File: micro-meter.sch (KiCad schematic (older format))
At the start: 143 parts, among them J1 DC_IN, J10 5V_OUT, J2 SPI, J3 I2C / UART, J4 IN1, J5 IN2, J6 IN3, J7 IN4, J8 SWD, J9 USB_B_Micro, U1 MP2359, U2 STM32F411CEU6, U3 XC6206P332MR, U4 MCP6002-ISN, U5 USBLC6-2SC6, Y1 16MHz

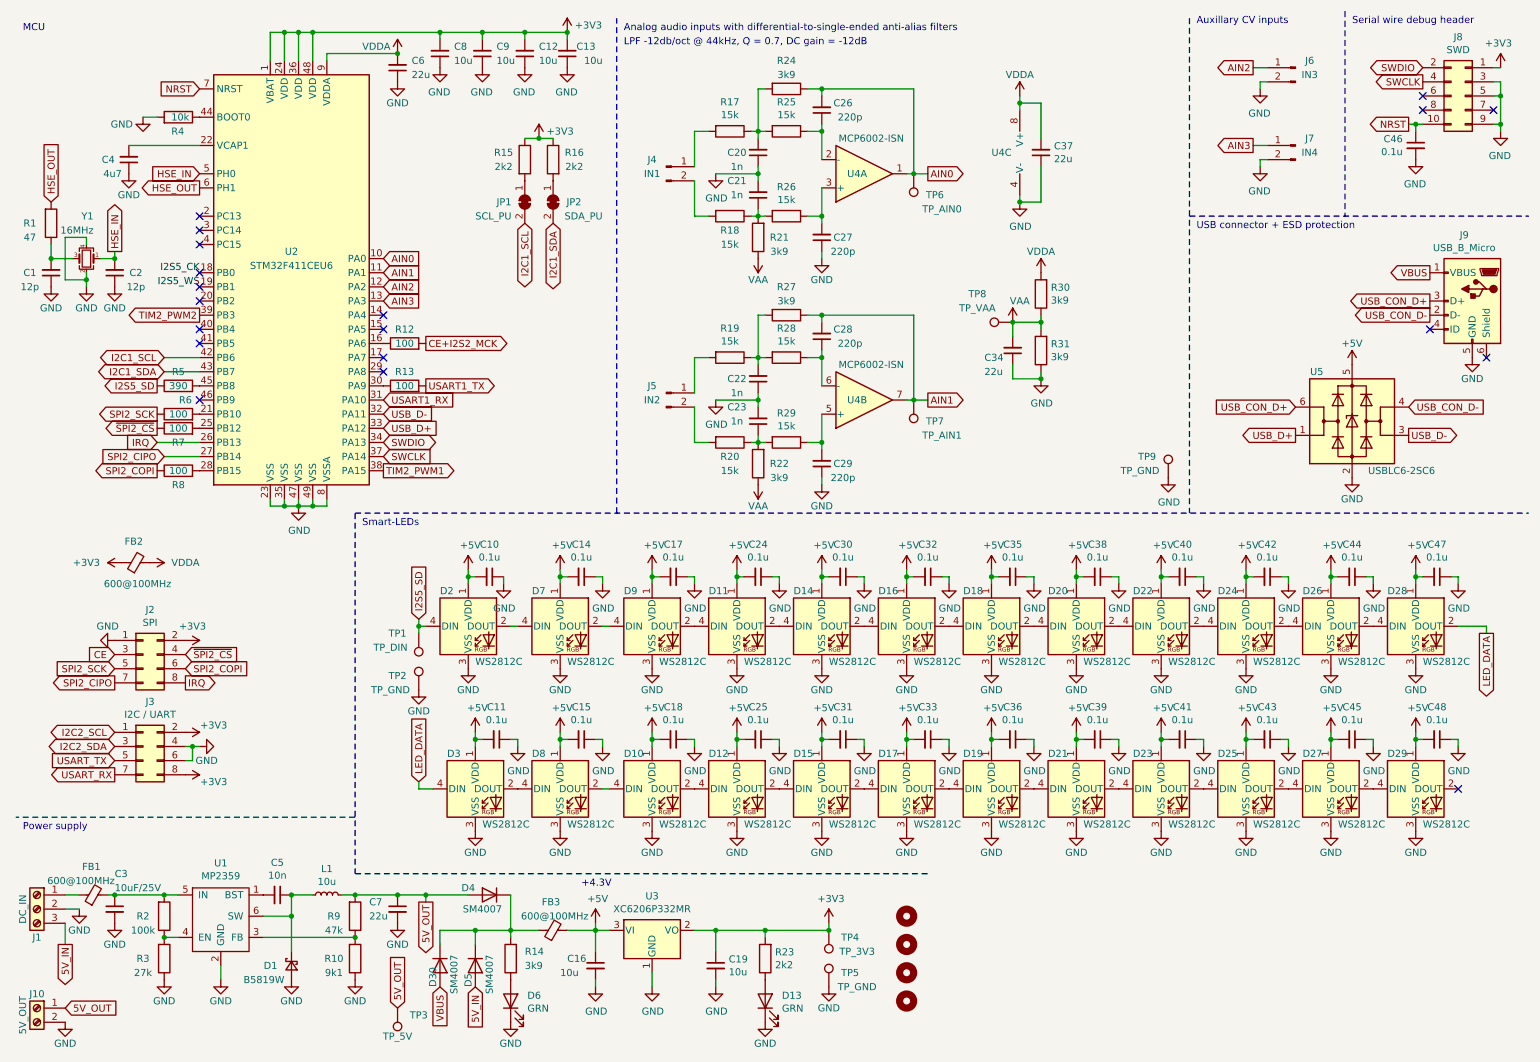
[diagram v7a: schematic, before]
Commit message: Change buck inductor value
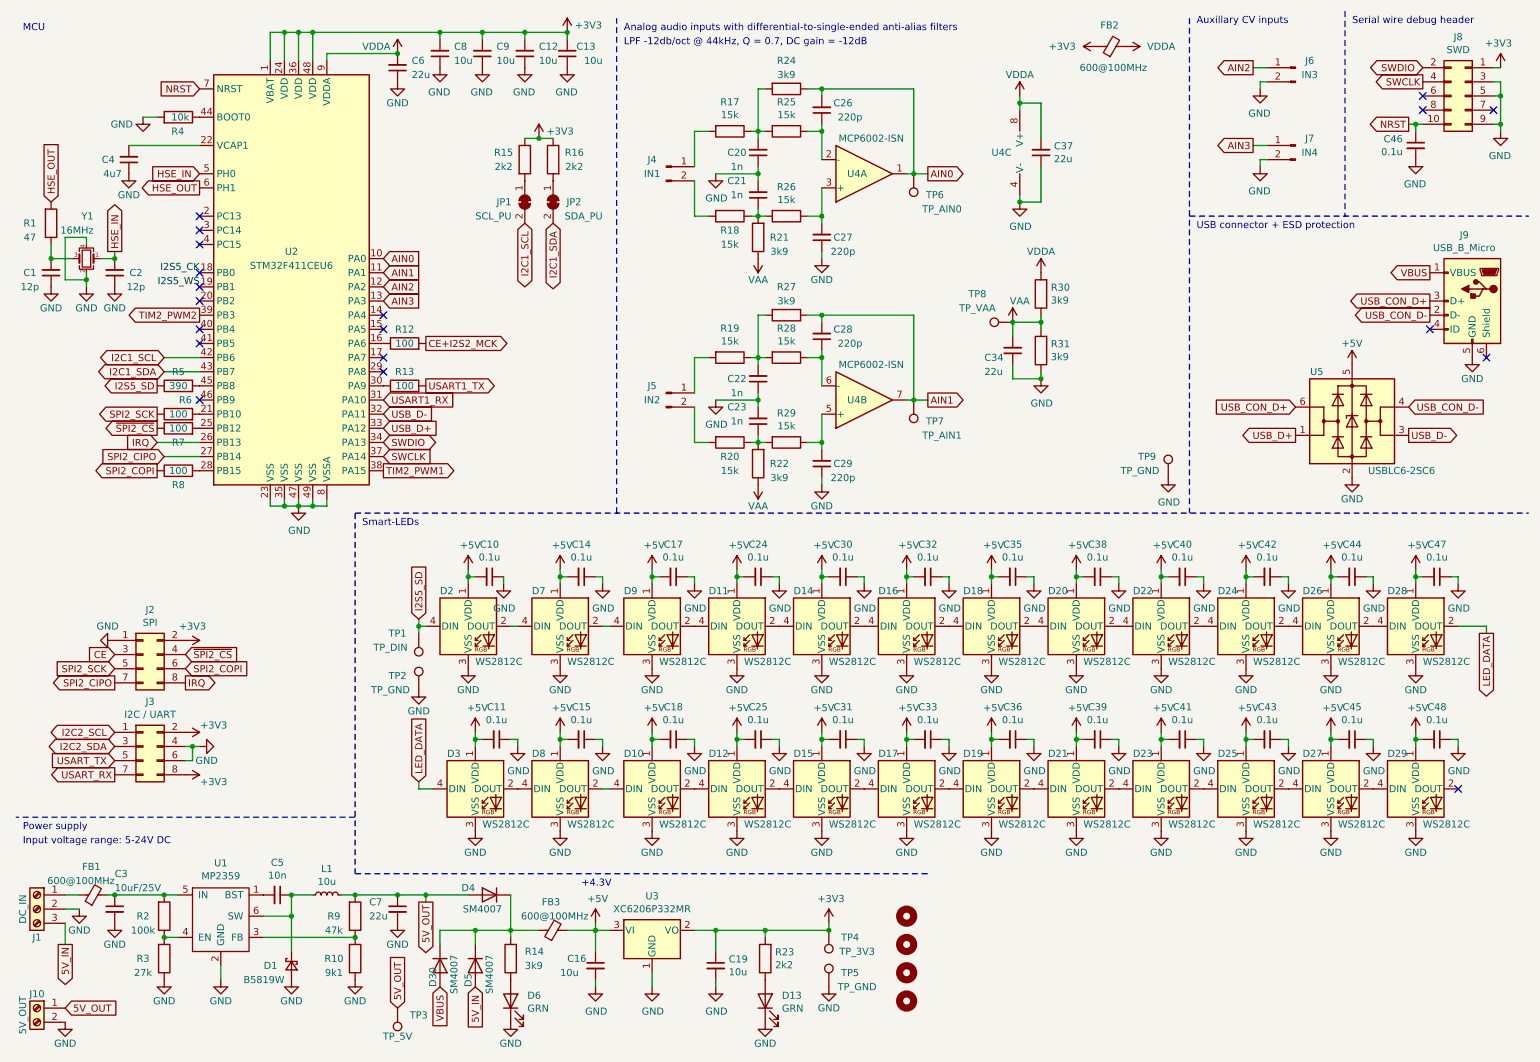
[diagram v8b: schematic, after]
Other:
- note added: "Input voltage range: 5-24V DC"
- moved on the sheet: FB2
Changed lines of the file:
@@
 L Device:Ferrite_Bead_Small FB2
 U 1 1 5FB88FB9
-P 1350 4350
-F 0 "FB2" V 1500 4300 50  0000 L CNN
-F 1 "600@100MHz" V 1200 4100 50  0000 L CNN
-F 2 "Inductor_SMD:L_0805_2012Metric" V 1280 4350 50  0001 C CNN
-F 3 "~" H 1350 4350 50  0001 C CNN
-	1    1350 4350
+P 8250 700
+F 0 "FB2" V 8400 650 50  0000 L CNN
+F 1 "600@100MHz" V 8100 450 50  0000 L CNN
+F 2 "Inductor_SMD:L_0805_2012Metric" V 8180 700 50  0001 C CNN
+F 3 "~" H 8250 700 50  0001 C CNN
+	1    8250 700
 	0    -1   -1   0
 $EndComp
@@
 L power:+3V3 #PWR07
 U 1 1 600F9CF0
-P 1250 4350
-F 0 "#PWR07" H 1250 4200 50  0001 C CNN
-F 1 "+3V3" V 1250 4600 50  0000 C CNN
-F 2 "" H 1250 4350 50  0001 C CNN
-F 3 "" H 1250 4350 50  0001 C CNN
-	1    1250 4350
+P 8150 700
+F 0 "#PWR07" H 8150 550 50  0001 C CNN
+F 1 "+3V3" V 8150 950 50  0000 C CNN
+F 2 "" H 8150 700 50  0001 C CNN
+F 3 "" H 8150 700 50  0001 C CNN
+	1    8150 700
 	0    -1   -1   0
 $EndComp
@@
 L power:VDDA #PWR010
 U 1 1 600E5FF4
-P 1450 4350
-F 0 "#PWR010" H 1450 4200 50  0001 C CNN
-F 1 "VDDA" V 1450 4600 50  0000 C CNN
-F 2 "" H 1450 4350 50  0001 C CNN
-F 3 "" H 1450 4350 50  0001 C CNN
-	1    1450 4350
+P 8350 700
+F 0 "#PWR010" H 8350 550 50  0001 C CNN
+F 1 "VDDA" V 8350 950 50  0000 C CNN
+F 2 "" H 8350 700 50  0001 C CNN
+F 3 "" H 8350 700 50  0001 C CNN
+	1    8350 700
 	0    1    1    0
 $EndComp
@@
 $EndComp
 $Comp
-L Device:L_Small L1
-U 1 1 60104FC2
-P 2700 6700
-F 0 "L1" V 2885 6700 50  0000 C CNN
-F 1 "10u" V 2794 6700 50  0000 C CNN
-F 2 "Inductor_SMD:L_Sunlord_MWSA0518_5.4x5.2mm" H 2700 6700 50  0001 C CNN
-F 3 "~" H 2700 6700 50  0001 C CNN
-	1    2700 6700
-	0    -1   -1   0
-$EndComp
-$Comp
 L power:GND #PWR017
 U 1 1 60104A85
@@
 Wire Wire Line
 	3400 6700 3700 6700
+$Comp
+L Device:L_Small L1
+U 1 1 60104FC2
+P 2700 6700
+F 0 "L1" V 2885 6700 50  0000 C CNN
+F 1 "10u" V 2794 6700 50  0000 C CNN
+F 2 "Inductor_SMD:L_Sunlord_MWSA0518_5.4x5.2mm" H 2700 6700 50  0001 C CNN
+F 3 "~" H 2700 6700 50  0001 C CNN
+	1    2700 6700
+	0    -1   -1   0
+$EndComp
+Text Notes 550  6350 0    50   ~ 0
+Input voltage range: 5-24V DC
 $EndSCHEMATC
